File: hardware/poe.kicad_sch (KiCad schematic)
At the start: 33 parts, among them T2 HR051067, U10 EL357N(B)(TA)-G, U11 CJ431, U9 Si3402-B

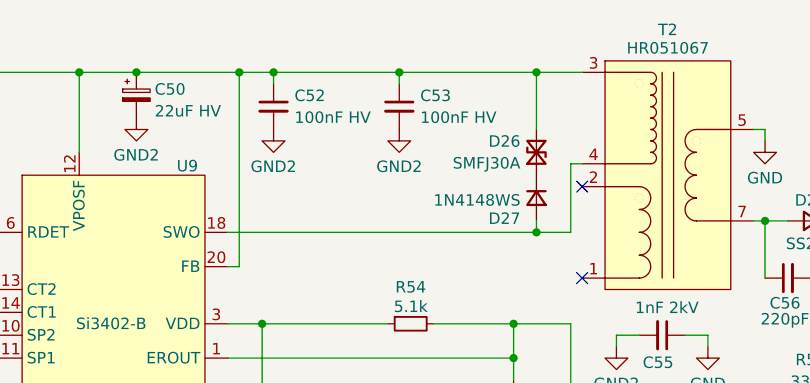
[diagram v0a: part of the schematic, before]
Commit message: hardware: switch to ESP32-C3 MCU and Si3402-B for PoE
Further changes:
 - Enlarge center hole to 16mm diameter
 - Replace Ethernet Phy by KSZ8851 SPI MAC + Phy
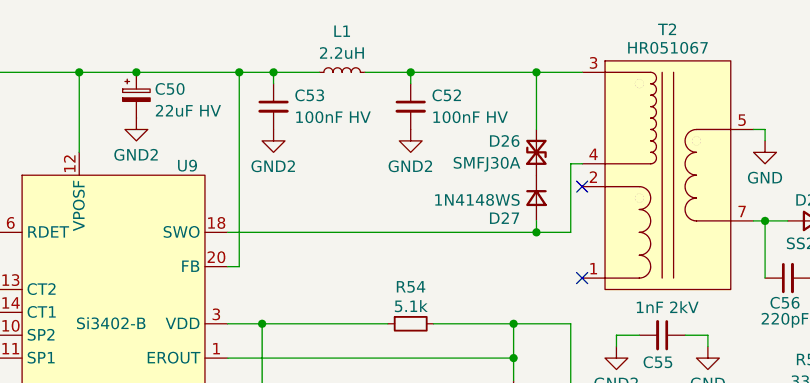
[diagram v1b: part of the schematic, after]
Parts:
- added L1: 2.2uH, Inductor_SMD:L_1008_2520Metric, symbol Device:L_Small
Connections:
- net at C49.1, C50.1, C53.1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: now also L1.1; no longer C52.1, D26.2 (A2), T2.3
- new net: C52.1, D26.2 (A2), L1.2, T2.3
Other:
- moved on the sheet: C52, C53
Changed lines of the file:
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@@
 	(paper "A4")
 	(junction
-		(at 135.89 76.2)
+		(at 176.53 123.19)
 		(diameter 0)
 		(color 0 0 0 0)
 	)
 	(junction
-		(at 176.53 123.19)
+		(at 121.92 76.2)
 		(diameter 0)
 		(color 0 0 0 0)
@@
 	)
 	(junction
-		(at 121.92 76.2)
+		(at 137.16 76.2)
 		(diameter 0)
 		(color 0 0 0 0)
@@
 	(wire
 		(pts
-			(xy 88.9 102.87) (xy 88.9 101.6)
+			(xy 132.08 76.2) (xy 137.16 76.2)
 		)
 		(stroke
@@
 	(wire
 		(pts
-			(xy 212.09 92.71) (xy 212.09 113.03)
+			(xy 88.9 102.87) (xy 88.9 101.6)
 		)
 		(stroke
@@
 	(wire
 		(pts
-			(xy 88.9 107.95) (xy 88.9 106.68)
+			(xy 212.09 92.71) (xy 212.09 113.03)
 		)
 		(stroke
@@
 	(wire
 		(pts
-			(xy 184.15 113.03) (xy 212.09 113.03)
+			(xy 88.9 107.95) (xy 88.9 106.68)
 		)
 		(stroke
@@
 	(wire
 		(pts
-			(xy 135.89 76.2) (xy 151.13 76.2)
+			(xy 184.15 113.03) (xy 212.09 113.03)
 		)
 		(stroke
@@
 	(wire
 		(pts
-			(xy 135.89 76.2) (xy 135.89 77.47)
+			(xy 137.16 76.2) (xy 137.16 77.47)
 		)
 		(stroke
@@
 	(wire
 		(pts
+			(xy 121.92 76.2) (xy 127 76.2)
+		)
+		(stroke
+			(width 0)
+			(type default)
+		)
+	)
+	(wire
+		(pts
 			(xy 105.41 124.46) (xy 107.95 124.46)
 		)
@@
 	(wire
 		(pts
-			(xy 212.09 92.71) (xy 201.93 92.71)
+			(xy 137.16 76.2) (xy 151.13 76.2)
 		)
 		(stroke
@@
 	(wire
 		(pts
-			(xy 100.33 76.2) (xy 100.33 85.09)
+			(xy 212.09 92.71) (xy 201.93 92.71)
 		)
 		(stroke
@@
 	(wire
 		(pts
-			(xy 106.68 76.2) (xy 100.33 76.2)
+			(xy 100.33 76.2) (xy 100.33 85.09)
 		)
 		(stroke
@@
 	(wire
 		(pts
-			(xy 88.9 106.68) (xy 88.9 105.41)
+			(xy 106.68 76.2) (xy 100.33 76.2)
 		)
 		(stroke
@@
 	(wire
 		(pts
-			(xy 139.7 104.14) (xy 148.59 104.14)
+			(xy 88.9 106.68) (xy 88.9 105.41)
 		)
 		(stroke
@@
 	(wire
 		(pts
-			(xy 154.94 118.11) (xy 154.94 104.14)
+			(xy 139.7 104.14) (xy 148.59 104.14)
 		)
 		(stroke
@@
 	(wire
 		(pts
-			(xy 60.96 124.46) (xy 67.31 124.46)
+			(xy 154.94 118.11) (xy 154.94 104.14)
 		)
 		(stroke
@@
 	(wire
 		(pts
-			(xy 212.09 92.71) (xy 213.36 92.71)
+			(xy 60.96 124.46) (xy 67.31 124.46)
 		)
 		(stroke
@@
 	(wire
 		(pts
-			(xy 121.92 76.2) (xy 135.89 76.2)
+			(xy 212.09 92.71) (xy 213.36 92.71)
 		)
 		(stroke
@@
 	(symbol
 		(lib_id "Device:C_Small")
-		(at 121.92 80.01 0)
+		(at 137.16 80.01 0)
 		(unit 1)
 		(exclude_from_sim no)
@@
 		(dnp no)
 		(property "Reference" "C52"
-			(at 124.2441 78.8041 0)
+			(at 139.4841 78.8041 0)
 			(effects
 				(font
@@
 		)
 		(property "Value" "100nF HV"
-			(at 124.2441 81.2284 0)
+			(at 139.4841 81.2284 0)
 			(effects
 				(font
@@
 		)
 		(property "Footprint" "Capacitor_SMD:C_0805_2012Metric"
-			(at 121.92 80.01 0)
+			(at 137.16 80.01 0)
 			(effects
 				(font
@@
 		)
 		(property "Datasheet" "~"
-			(at 121.92 80.01 0)
+			(at 137.16 80.01 0)
 			(effects
 				(font
@@
 		)
 		(property "Description" "Unpolarized capacitor, small symbol"
-			(at 121.92 80.01 0)
+			(at 137.16 80.01 0)
 			(effects
 				(font
@@
 		)
 		(property "LCSC" "C28233"
-			(at 121.92 80.01 0)
+			(at 137.16 80.01 0)
 			(effects
 				(font
@@
 	)
 	(symbol
+		(lib_id "Device:L_Small")
+		(at 129.54 76.2 90)
+		(unit 1)
+		(exclude_from_sim no)
+		(in_bom yes)
+		(on_board yes)
+		(dnp no)
+		(fields_autoplaced yes)
+		(property "Reference" "L1"
+			(at 129.54 71.6767 90)
+			(effects
+				(font
+					(size 1.27 1.27)
+				)
+			)
+		)
+		(property "Value" "2.2uH"
+			(at 129.54 74.101 90)
+			(effects
+				(font
+					(size 1.27 1.27)
+				)
+			)
+		)
+		(property "Footprint" "Inductor_SMD:L_1008_2520Metric"
+			(at 129.54 76.2 0)
+			(effects
+				(font
+					(size 1.27 1.27)
+				)
+				(hide yes)
+			)
+		)
+		(property "Datasheet" "~"
+			(at 129.54 76.2 0)
+			(effects
+				(font
+					(size 1.27 1.27)
+				)
+				(hide yes)
+			)
+		)
+		(property "Description" "Inductor, small symbol"
+			(at 129.54 76.2 0)
+			(effects
+				(font
+					(size 1.27 1.27)
+				)
+				(hide yes)
+			)
+		)
+		(property "LCSC" "C964122"
+			(at 129.54 76.2 90)
+			(effects
+				(font
+					(size 1.27 1.27)
+				)
+				(hide yes)
+			)
+		)
+		(pin "1"
+		)
+		(pin "2"
+		)
+		(instances
+			(project "TallyLight"
+				(path "/d4f869dd-5485-4b4f-b239-21313c2a8e4c/210de0db-26c5-4c02-8853-8d735ccb28a9"
+					(reference "L1")
+					(unit 1)
+				)
+			)
+		)
+	)
+	(symbol
 		(lib_id "power:GND2")
 		(at 148.59 125.73 0)
@@
 	(symbol
 		(lib_id "power:GND2")
-		(at 135.89 82.55 0)
+		(at 137.16 82.55 0)
 		(unit 1)
 		(exclude_from_sim no)
@@
 		(fields_autoplaced yes)
 		(property "Reference" "#PWR099"
-			(at 135.89 88.9 0)
+			(at 137.16 88.9 0)
 			(effects
 				(font
@@
 		)
 		(property "Value" "GND2"
-			(at 135.89 86.6831 0)
+			(at 137.16 86.6831 0)
 			(effects
 				(font
@@
 		)
 		(property "Footprint" ""
-			(at 135.89 82.55 0)
+			(at 137.16 82.55 0)
 			(effects
 				(font
@@
 		)
 		(property "Datasheet" ""
-			(at 135.89 82.55 0)
+			(at 137.16 82.55 0)
 			(effects
 				(font
@@
 		)
 		(property "Description" "Power symbol creates a global label with name \"GND2\" , ground"
-			(at 135.89 82.55 0)
+			(at 137.16 82.55 0)
 			(effects
 				(font
@@
 	(symbol
 		(lib_id "Device:C_Small")
-		(at 135.89 80.01 0)
+		(at 121.92 80.01 0)
 		(unit 1)
 		(exclude_from_sim no)
@@
 		(dnp no)
 		(property "Reference" "C53"
-			(at 138.2141 78.8041 0)
+			(at 124.2441 78.8041 0)
 			(effects
 				(font
@@
 		)
 		(property "Value" "100nF HV"
-			(at 138.2141 81.2284 0)
+			(at 124.2441 81.2284 0)
 			(effects
 				(font
@@
 		)
 		(property "Footprint" "Capacitor_SMD:C_0805_2012Metric"
-			(at 135.89 80.01 0)
+			(at 121.92 80.01 0)
 			(effects
 				(font
@@
 		)
 		(property "Datasheet" "~"
-			(at 135.89 80.01 0)
+			(at 121.92 80.01 0)
 			(effects
 				(font
@@
 		)
 		(property "Description" "Unpolarized capacitor, small symbol"
-			(at 135.89 80.01 0)
+			(at 121.92 80.01 0)
 			(effects
 				(font
@@
 		)
 		(property "LCSC" "C28233"
-			(at 135.89 80.01 0)
+			(at 121.92 80.01 0)
 			(effects
 				(font

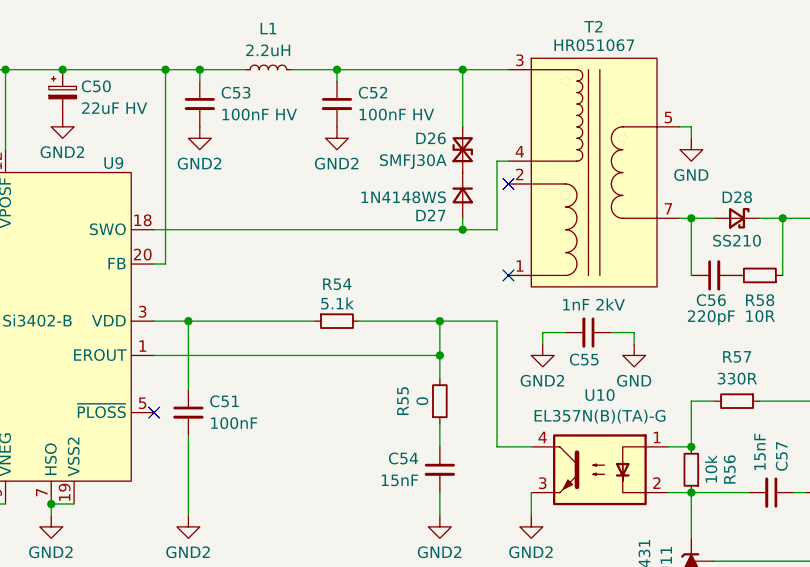
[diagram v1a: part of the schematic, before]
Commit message: hardware: replace ESP32-C3 MINI by more common WROOM-02 module
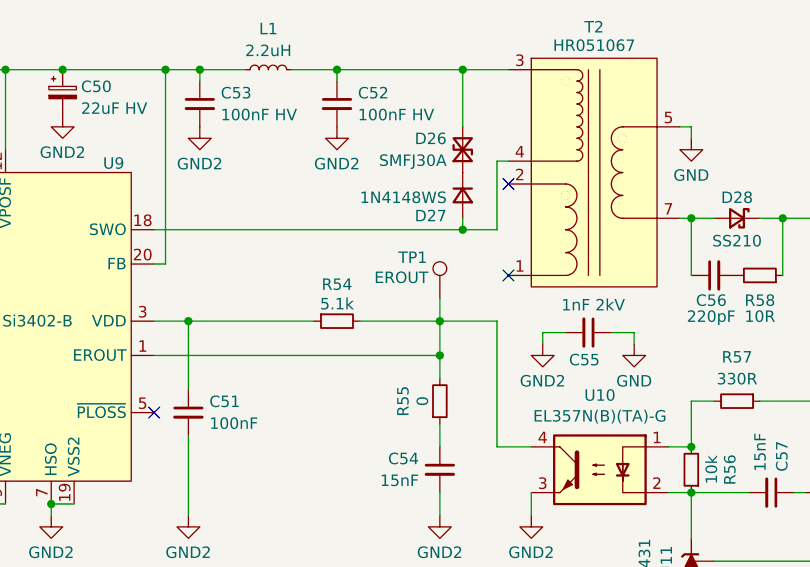
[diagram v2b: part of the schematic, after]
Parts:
- added TP1: EROUT, TestPoint:TestPoint_Pad_D2.0mm, symbol Connector:TestPoint
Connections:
- net at R54.2, R55.2, U10.4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: now also TP1.1
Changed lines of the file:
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@@
+	(wire
+		(pts
+			(xy 148.59 101.6) (xy 148.59 104.14)
+		)
+		(stroke
+			(width 0)
+			(type default)
+		)
+	)
 	(wire
 		(pts
@@
 					(unit 1)
 				)
+			)
+		)
+	)
+	(symbol
+		(lib_id "Connector:TestPoint")
+		(at 148.59 101.6 0)
+		(mirror y)
+		(unit 1)
+		(exclude_from_sim no)
+		(in_bom yes)
+		(on_board yes)
+		(dnp no)
+		(property "Reference" "TP1"
+			(at 147.193 97.0858 0)
+			(effects
+				(font
+					(size 1.27 1.27)
+				)
+				(justify left)
+			)
+		)
+		(property "Value" "EROUT"
+			(at 147.32 99.314 0)
+			(effects
+				(font
+					(size 1.27 1.27)
+				)
+				(justify left)
+			)
+		)
+		(property "Footprint" "TestPoint:TestPoint_Pad_D2.0mm"
+			(at 143.51 101.6 0)
+			(effects
+				(font
+					(size 1.27 1.27)
+				)
+				(hide yes)
+			)
+		)
+		(property "Datasheet" "~"
+			(at 143.51 101.6 0)
+			(effects
+				(font
+					(size 1.27 1.27)
+				)
+				(hide yes)
+			)
+		)
+		(property "Description" "test point"
+			(at 148.59 101.6 0)
+			(effects
+				(font
+					(size 1.27 1.27)
+				)
+				(hide yes)
+			)
+		)
+		(pin "1"
+		)
+		(instances
+			(project ""
+				(path "/d4f869dd-5485-4b4f-b239-21313c2a8e4c/210de0db-26c5-4c02-8853-8d735ccb28a9"
+					(reference "TP1")
+					(unit 1)
+				)

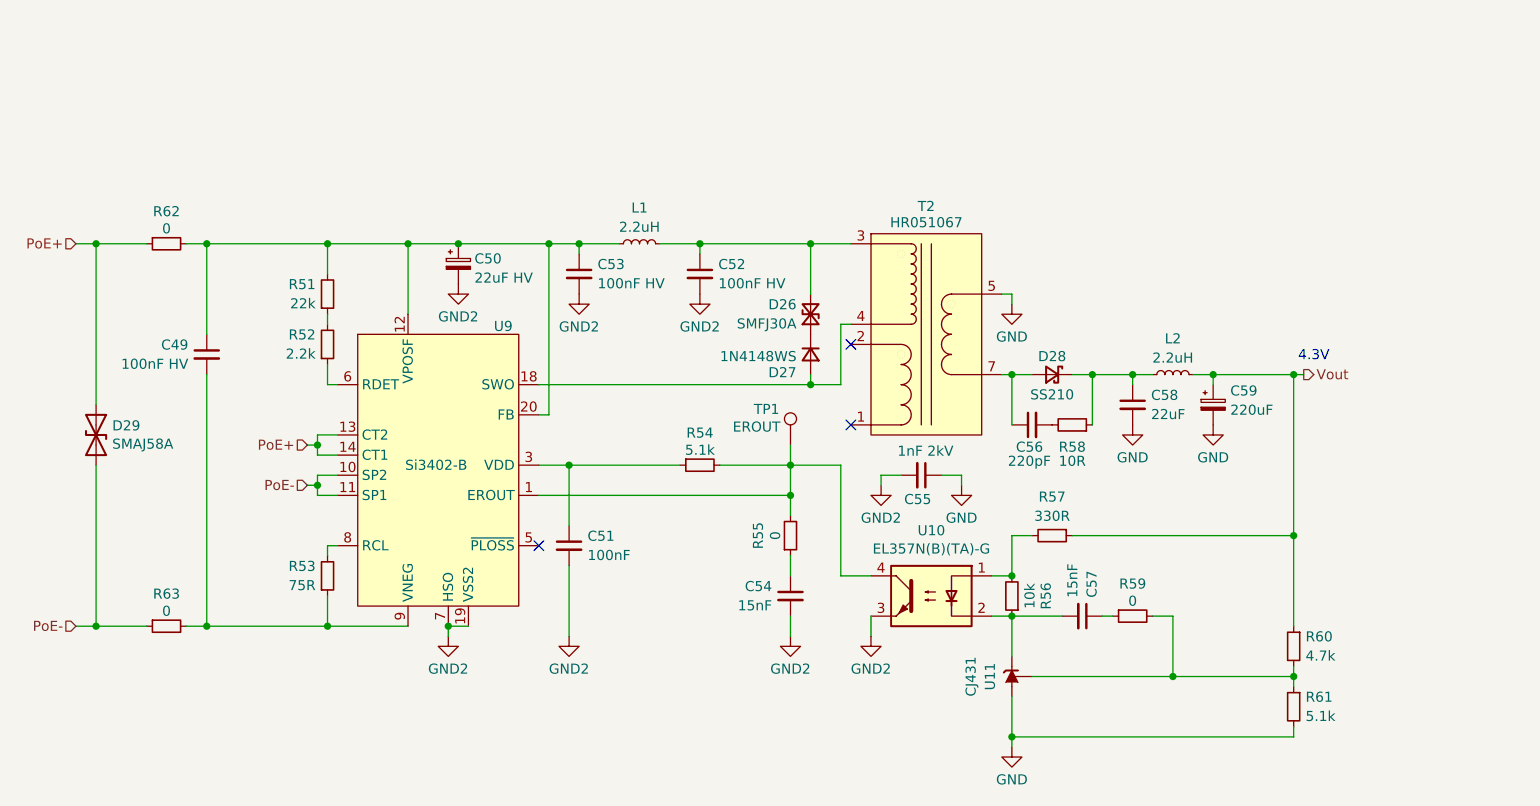
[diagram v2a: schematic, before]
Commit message: hardware: add testpoints to flyback converter and SPI MAC + Phy
Add testpoints to all critical section that might require in-circuit
debugging
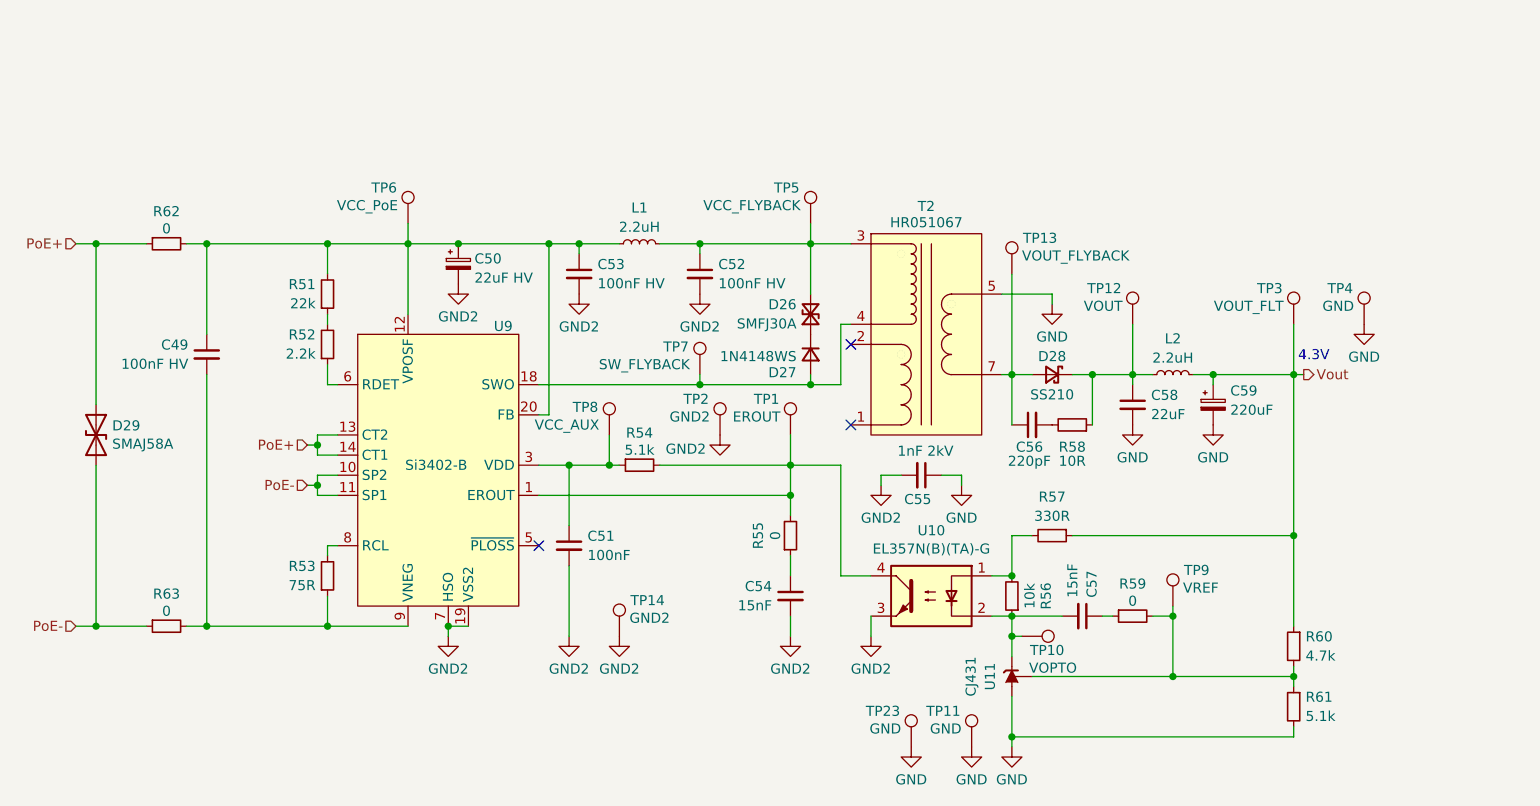
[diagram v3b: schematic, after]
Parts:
- added TP10: VOPTO, TestPoint_no_outline:TestPoint_Pad_D2.0mm_no_outline, symbol Connector:TestPoint
- added TP11, TP23, TP4: GND, TestPoint:TestPoint_Pad_D2.0mm, symbol Connector:TestPoint
- added TP12: VOUT, TestPoint_no_outline:TestPoint_Pad_D2.0mm_no_outline, symbol Connector:TestPoint
- added TP13: VOUT_FLYBACK, TestPoint_no_outline:TestPoint_Pad_D2.0mm_no_outline, symbol Connector:TestPoint
- added TP14, TP2: GND2, TestPoint_polygon_outline:TestPoint_Pad_D2.0mm_trianglular_outline, symbol Connector:TestPoint
- added TP3: VOUT_FLT, TestPoint_no_outline:TestPoint_Pad_D2.0mm_no_outline, symbol Connector:TestPoint
- added TP5: VCC_FLYBACK, TestPoint_no_outline:TestPoint_Pad_D2.0mm_no_outline, symbol Connector:TestPoint
- added TP6: VCC_PoE, TestPoint_no_outline:TestPoint_Pad_D2.0mm_no_outline, symbol Connector:TestPoint
- added TP7: SW_FLYBACK, TestPoint_no_outline:TestPoint_Pad_D2.0mm_no_outline, symbol Connector:TestPoint
- added TP8: VCC_AUX, TestPoint_no_outline:TestPoint_Pad_D2.0mm_no_outline, symbol Connector:TestPoint
- added TP9: VREF, TestPoint_no_outline:TestPoint_Pad_D2.0mm_no_outline, symbol Connector:TestPoint
- TP1: footprint TestPoint:TestPoint_Pad_D2.0mm -> TestPoint_no_outline:TestPoint_Pad_D2.0mm_no_outline
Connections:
- net GND: now also TP11.1, TP23.1, TP4.1
- net GND2: now also TP14.1, TP2.1
- net Vout: now also TP3.1
- net at R59.2, R60.2, R61.1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: now also TP9.1
- net at D27.2 (A), T2.4, U9.18 (SWO): now also TP7.1
- net at C56.1, D28.2 (A), T2.7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: now also TP13.1
- net at C51.1, R54.1, U9.3 (VDD): now also TP8.1
- net at C57.2, R56.1, U10.2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: now also TP10.1
- net at C58.1, D28.1 (K), L2.1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: now also TP12.1
- net at C52.1, D26.2 (A2), L1.2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: now also TP5.1
- net at C49.1, C50.1, C53.1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: now also TP6.1
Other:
- moved on the sheet: R54, TP1

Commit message: hardware: add alternate snubber and flyback footprints
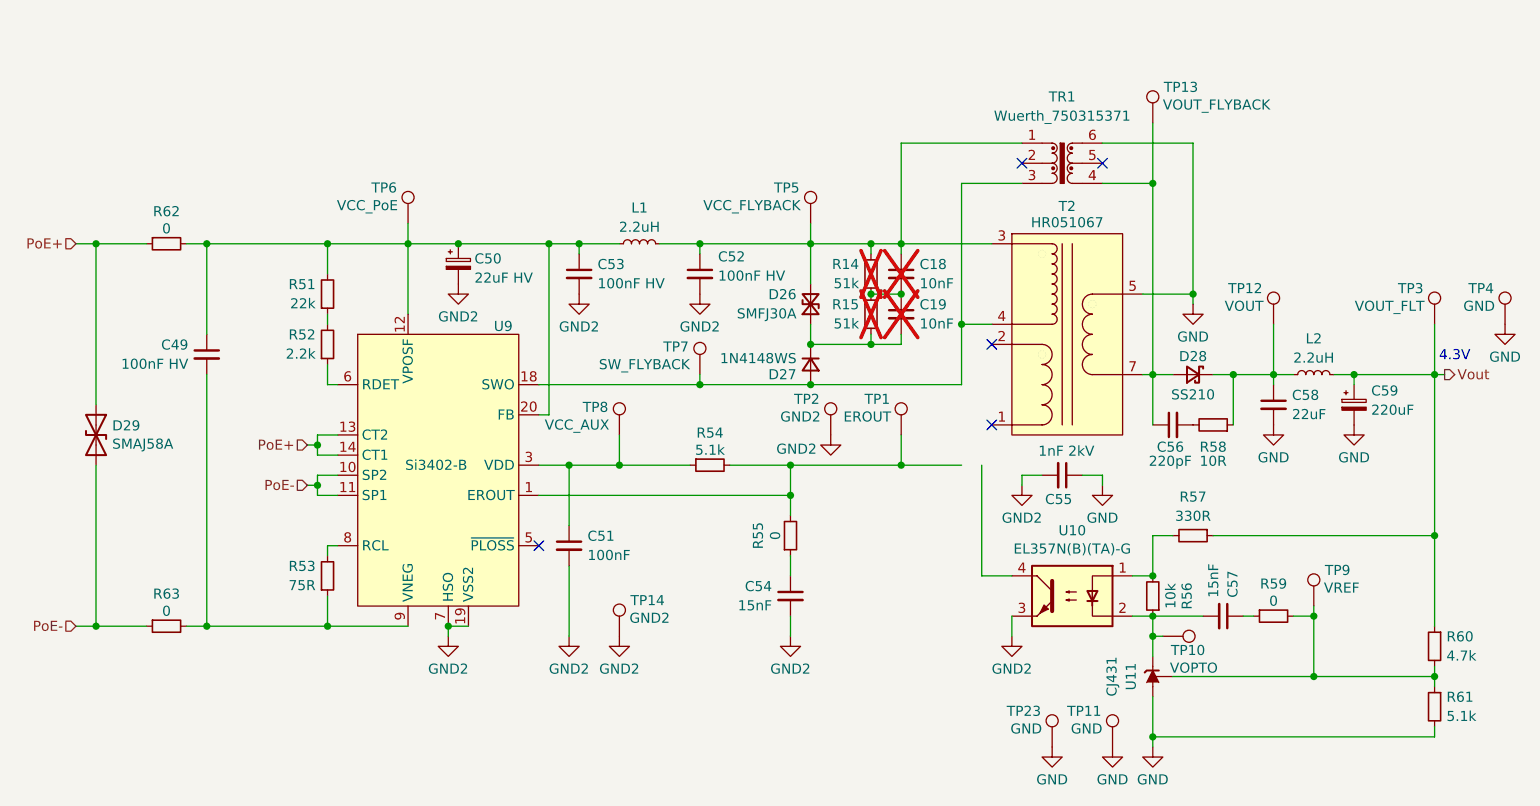
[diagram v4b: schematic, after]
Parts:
- added C18, C19: 10nF, Capacitor_SMD:C_0402_1005Metric, symbol Device:C_Small
- added R14, R15: 51k, Resistor_SMD:R_0402_1005Metric, symbol Device:R_Small
- added TR1: Wuerth_750315371, Transformer_SMD:Transformer_Wuerth_750315371, symbol Transformer:Wuerth_750315371
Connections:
- net GND: now also TR1.6
- net at D26.1 (A1), D27.1 (K): now also C19.2, R15.1
- net at D27.2 (A), T2.4, TP7.1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: now also TR1.3
- net at C56.1, D28.2 (A), T2.7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: now also TR1.4
- net at R54.2, R55.2, TP1.1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: no longer U10.4
- net at C52.1, D26.2 (A2), L1.2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: now also C18.1, R14.2, TR1.1
- new net: C18.2, C19.1, R14.1, R15.2
- no-connect marks 3 -> 5
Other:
- moved on the sheet: C55, C56, C57, C58, C59, D26, D27, D28, L2, R54, R56, R57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
